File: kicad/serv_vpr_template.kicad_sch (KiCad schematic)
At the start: 89 parts, among them J1 Conn_01x02_Pin

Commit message: add remaining IOs to template
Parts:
- added D49, D50, D51, D52, D53, D54, D55, D56, D57, D58, D59, D60, D61, D62, D63, D64, D65, D66, D67, D68, D69, D70, D71, D72: ~, LED_THT:LED_D5.0mm, symbol Device:LED
- added RN21, RN22, RN23, RN24, RN25, RN26: SIL 8-4 1,0K, Resistor_THT:R_Array_SIP8, symbol serv_vpr_template:R_Pack04_SIL
- D36: now not fitted
- SW1, SW12, SW13, SW2, SW3: symbol Switch:SW_MEC_5G -> Switch:SW_Push
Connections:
- net GND: now also SW1.2, RN21.2 (R1.2), RN21.4 (R2.2), RN21.6 (R3.2), RN21.8 (R4.2), RN22.2 (R1.2), RN22.4 (R2.2), RN22.6 (R3.2), RN22.8 (R4.2), RN23.2 (R1.2), RN23.4 (R2.2), RN23.6 (R3.2), RN23.8 (R4.2), RN24.2 (R1.2), RN24.4 (R2.2), RN24.6 (R3.2), RN24.8 (R4.2), RN25.2 (R1.2), RN25.4 (R2.2), RN25.6 (R3.2), RN25.8 (R4.2), RN26.2 (R1.2), RN26.4 (R2.2), RN26.6 (R3.2), RN26.8 (R4.2); no longer SW1.3 (B), SW1.4 (B)
- net VCC: now also SW12.2, SW13.2, SW2.2, SW3.2; no longer SW12.3 (B), SW12.4 (B), SW13.3 (B), SW13.4 (B), SW2.3 (B), SW2.4 (B), SW3.3 (B), SW3.4 (B)
- net d_dbus_ack: no longer SW13.2 (A)
- net i_dbus_ack: no longer SW12.2 (A)
- net i_ibus_rdt_0: now also RN4.9 (R8), SW7.9; no longer RN1.2 (R1), SW4.16
- net i_rst: no longer SW2.2 (A)
- net i_timer_irq: no longer SW3.2 (A)
- net o_dbus_sel_0: now also D40.2 (A); no longer D37.2 (A)
- net o_dbus_sel_1: now also D39.2 (A); no longer D38.2 (A)
- net o_dbus_sel_2: now also D38.2 (A); no longer D39.2 (A)
- net o_dbus_sel_3: now also D37.2 (A); no longer D40.2 (A)
- net at R1.2, R6.2, SW1.1: no longer SW1.2 (A)
- net i_ibus_rdt_1: now reaches RN4.8 (R7), SW7.10
- new net: D58.1 (K), RN23.3 (R2.1)
- new net: D56.1 (K), RN22.7 (R4.1)
- new net: D62.1 (K), RN24.3 (R2.1)
- new net: D71.1 (K), RN26.5 (R3.1)
- new net: D53.1 (K), RN22.1 (R1.1)
- new net: D54.1 (K), RN22.3 (R2.1)
- new net: D55.1 (K), RN22.5 (R3.1)
- new net: D49.1 (K), RN21.1 (R1.1)
- new net: D50.1 (K), RN21.3 (R2.1)
- new net: D51.1 (K), RN21.5 (R3.1)
- new net: D52.1 (K), RN21.7 (R4.1)
- new net: D65.1 (K), RN25.1 (R1.1)
- new net: D59.1 (K), RN23.5 (R3.1)
- new net: D66.1 (K), RN25.3 (R2.1)
- new net: D63.1 (K), RN24.5 (R3.1)
- new net: D61.1 (K), RN24.1 (R1.1)
- new net: D70.1 (K), RN26.3 (R2.1)
- new net: D69.1 (K), RN26.1 (R1.1)
- new net: D64.1 (K), RN24.7 (R4.1)
- new net: D72.1 (K), RN26.7 (R4.1)
- new net: D68.1 (K), RN25.7 (R4.1)
- new net: D57.1 (K), RN23.1 (R1.1)
- new net: D60.1 (K), RN23.7 (R4.1)
- new net: D67.1 (K), RN25.5 (R3.1)
- new net i_ibus_rdt_31: RN1.2 (R1), SW4.16
- new net o_dbus_dat_0: D72.2 (A)
- new net o_dbus_dat_1: D70.2 (A)
- new net o_dbus_dat_10: D60.2 (A)
- new net o_dbus_dat_11: D58.2 (A)
- new net o_dbus_dat_12: D63.2 (A)
- new net o_dbus_dat_13: D61.2 (A)
- new net o_dbus_dat_14: D59.2 (A)
- new net o_dbus_dat_15: D57.2 (A)
- new net o_dbus_dat_16: D56.2 (A)
- new net o_dbus_dat_17: D54.2 (A)
- new net o_dbus_dat_18: D52.2 (A)
- new net o_dbus_dat_19: D50.2 (A)
- new net o_dbus_dat_2: D68.2 (A)
- new net o_dbus_dat_20: D55.2 (A)
- new net o_dbus_dat_21: D53.2 (A)
- new net o_dbus_dat_22: D51.2 (A)
- new net o_dbus_dat_23: D49.2 (A)
- new net o_dbus_dat_3: D66.2 (A)
- new net o_dbus_dat_4: D71.2 (A)
- new net o_dbus_dat_5: D69.2 (A)
- new net o_dbus_dat_6: D67.2 (A)
- new net o_dbus_dat_7: D65.2 (A)
- new net o_dbus_dat_8: D64.2 (A)
- new net o_dbus_dat_9: D62.2 (A)

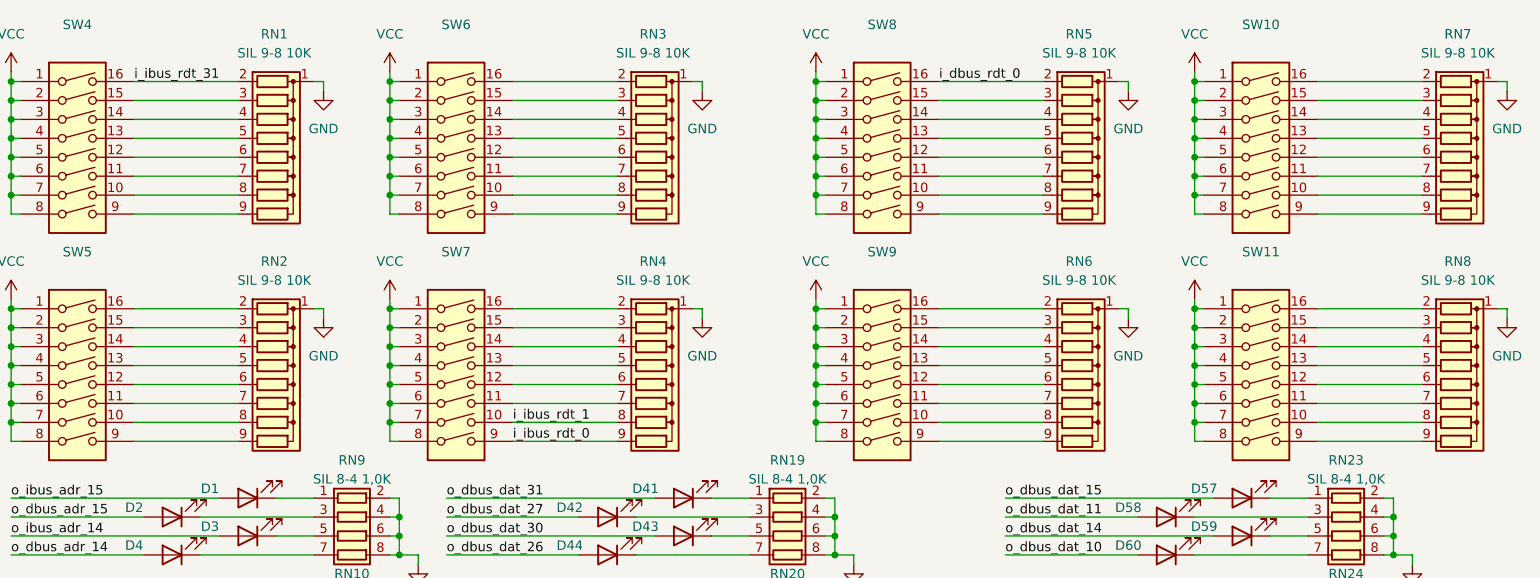
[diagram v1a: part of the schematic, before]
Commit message: connect ibus/dbus read data in template
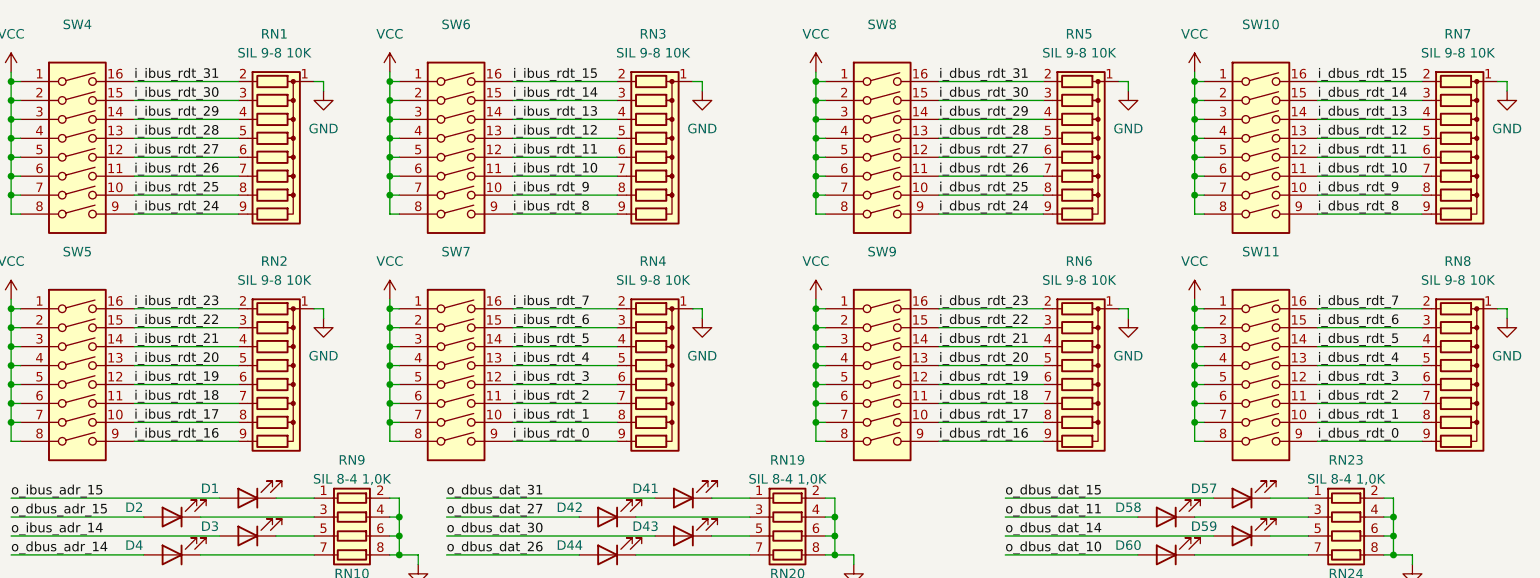
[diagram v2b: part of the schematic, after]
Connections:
- net i_dbus_rdt_0: now also RN8.9 (R8), SW11.9; no longer RN5.2 (R1), SW8.16
- net i_dbus_rdt_30: now reaches RN5.3 (R2), SW8.15
- net i_dbus_rdt_29: now reaches RN5.4 (R3), SW8.14
- net i_dbus_rdt_28: now reaches RN5.5 (R4), SW8.13
- net i_dbus_rdt_27: now reaches RN5.6 (R5), SW8.12
- net i_dbus_rdt_26: now reaches RN5.7 (R6), SW8.11
- net i_dbus_rdt_25: now reaches RN5.8 (R7), SW8.10
- net i_dbus_rdt_24: now reaches RN5.9 (R8), SW8.9
- net i_ibus_rdt_7: now reaches RN4.2 (R1), SW7.16
- net i_ibus_rdt_6: now reaches RN4.3 (R2), SW7.15
- net i_ibus_rdt_5: now reaches RN4.4 (R3), SW7.14
- net i_ibus_rdt_4: now reaches RN4.5 (R4), SW7.13
- net i_ibus_rdt_3: now reaches RN4.6 (R5), SW7.12
- net i_ibus_rdt_2: now reaches RN4.7 (R6), SW7.11
- net i_dbus_rdt_23: now reaches RN6.2 (R1), SW9.16
- net i_dbus_rdt_22: now reaches RN6.3 (R2), SW9.15
- net i_dbus_rdt_21: now reaches RN6.4 (R3), SW9.14
- net i_dbus_rdt_20: now reaches RN6.5 (R4), SW9.13
- net i_dbus_rdt_19: now reaches RN6.6 (R5), SW9.12
- net i_dbus_rdt_18: now reaches RN6.7 (R6), SW9.11
- net i_dbus_rdt_17: now reaches RN6.8 (R7), SW9.10
- net i_dbus_rdt_16: now reaches RN6.9 (R8), SW9.9
- net i_dbus_rdt_7: now reaches RN8.2 (R1), SW11.16
- net i_dbus_rdt_6: now reaches RN8.3 (R2), SW11.15
- net i_dbus_rdt_5: now reaches RN8.4 (R3), SW11.14
- net i_dbus_rdt_4: now reaches RN8.5 (R4), SW11.13
- net i_dbus_rdt_3: now reaches RN8.6 (R5), SW11.12
- net i_dbus_rdt_2: now reaches RN8.7 (R6), SW11.11
- net i_dbus_rdt_1: now reaches RN8.8 (R7), SW11.10
- net i_ibus_rdt_17: now reaches RN2.8 (R7), SW5.10
- net i_ibus_rdt_18: now reaches RN2.7 (R6), SW5.11
- net i_ibus_rdt_19: now reaches RN2.6 (R5), SW5.12
- net i_ibus_rdt_20: now reaches RN2.5 (R4), SW5.13
- net i_ibus_rdt_21: now reaches RN2.4 (R3), SW5.14
- net i_ibus_rdt_22: now reaches RN2.3 (R2), SW5.15
- net i_ibus_rdt_23: now reaches RN2.2 (R1), SW5.16
- net i_ibus_rdt_16: now reaches RN2.9 (R8), SW5.9
- net i_dbus_rdt_15: now reaches RN7.2 (R1), SW10.16
- net i_dbus_rdt_14: now reaches RN7.3 (R2), SW10.15
- net i_dbus_rdt_13: now reaches RN7.4 (R3), SW10.14
- net i_dbus_rdt_12: now reaches RN7.5 (R4), SW10.13
- net i_dbus_rdt_11: now reaches RN7.6 (R5), SW10.12
- net i_dbus_rdt_10: now reaches RN7.7 (R6), SW10.11
- net i_dbus_rdt_9: now reaches RN7.8 (R7), SW10.10
- net i_dbus_rdt_8: now reaches RN7.9 (R8), SW10.9
- net i_ibus_rdt_15: now reaches RN3.2 (R1), SW6.16
- net i_ibus_rdt_14: now reaches RN3.3 (R2), SW6.15
- net i_ibus_rdt_13: now reaches RN3.4 (R3), SW6.14
- net i_ibus_rdt_12: now reaches RN3.5 (R4), SW6.13
- net i_ibus_rdt_11: now reaches RN3.6 (R5), SW6.12
- net i_ibus_rdt_10: now reaches RN3.7 (R6), SW6.11
- net i_ibus_rdt_9: now reaches RN3.8 (R7), SW6.10
- net i_ibus_rdt_8: now reaches RN3.9 (R8), SW6.9
- net i_ibus_rdt_25: now reaches RN1.8 (R7), SW4.10
- net i_ibus_rdt_26: now reaches RN1.7 (R6), SW4.11
- net i_ibus_rdt_27: now reaches RN1.6 (R5), SW4.12
- net i_ibus_rdt_28: now reaches RN1.5 (R4), SW4.13
- net i_ibus_rdt_29: now reaches RN1.4 (R3), SW4.14
- net i_ibus_rdt_30: now reaches RN1.3 (R2), SW4.15
- net i_ibus_rdt_24: now reaches RN1.9 (R8), SW4.9
- new net i_dbus_rdt_31: RN5.2 (R1), SW8.16
